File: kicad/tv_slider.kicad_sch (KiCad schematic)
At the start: 10 parts, among them J1 MC 1,5/2-G-3.81, J2 MC 1,5/6-G-3.81, J3 MC 1,5/4-G-3.81, J4 MC 1,5/3-G-3.81, J5 MC 1,5/3-G-3.81, J6 MC 1,5/3-G-3.81, J7 MC 1,5/3-G-3.81

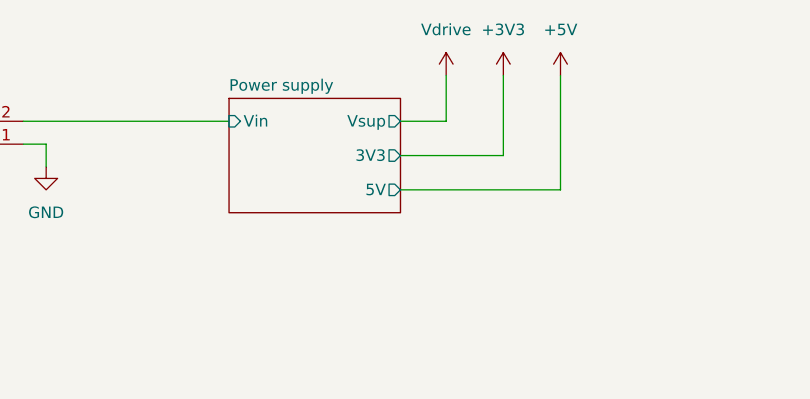
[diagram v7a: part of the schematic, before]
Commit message: Fixed up or explained all DRC violations.
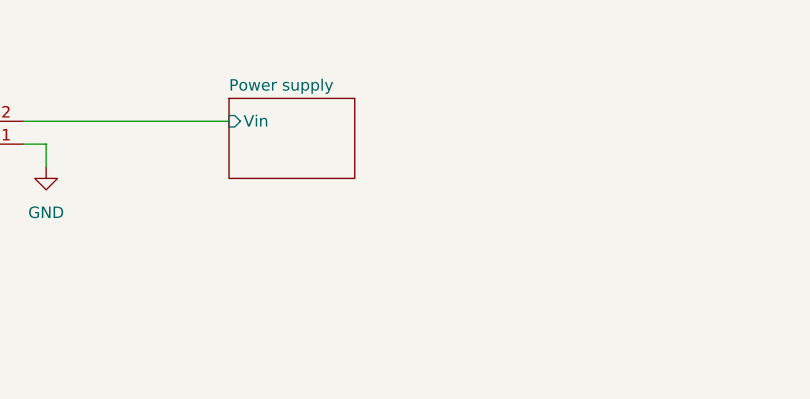
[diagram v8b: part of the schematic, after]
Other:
- sheet Power supply ports: added none; removed 3V3, 5V, Vsup
